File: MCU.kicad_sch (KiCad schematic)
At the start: 32 parts, among them J1 GT-USB-7010I, SW1 BOOT0, SW6 Reset, U1 STM32F722RETx, U2 AMS1117-3.3, X1 32.768kHz 7pF, Y1 16MHz 10pF

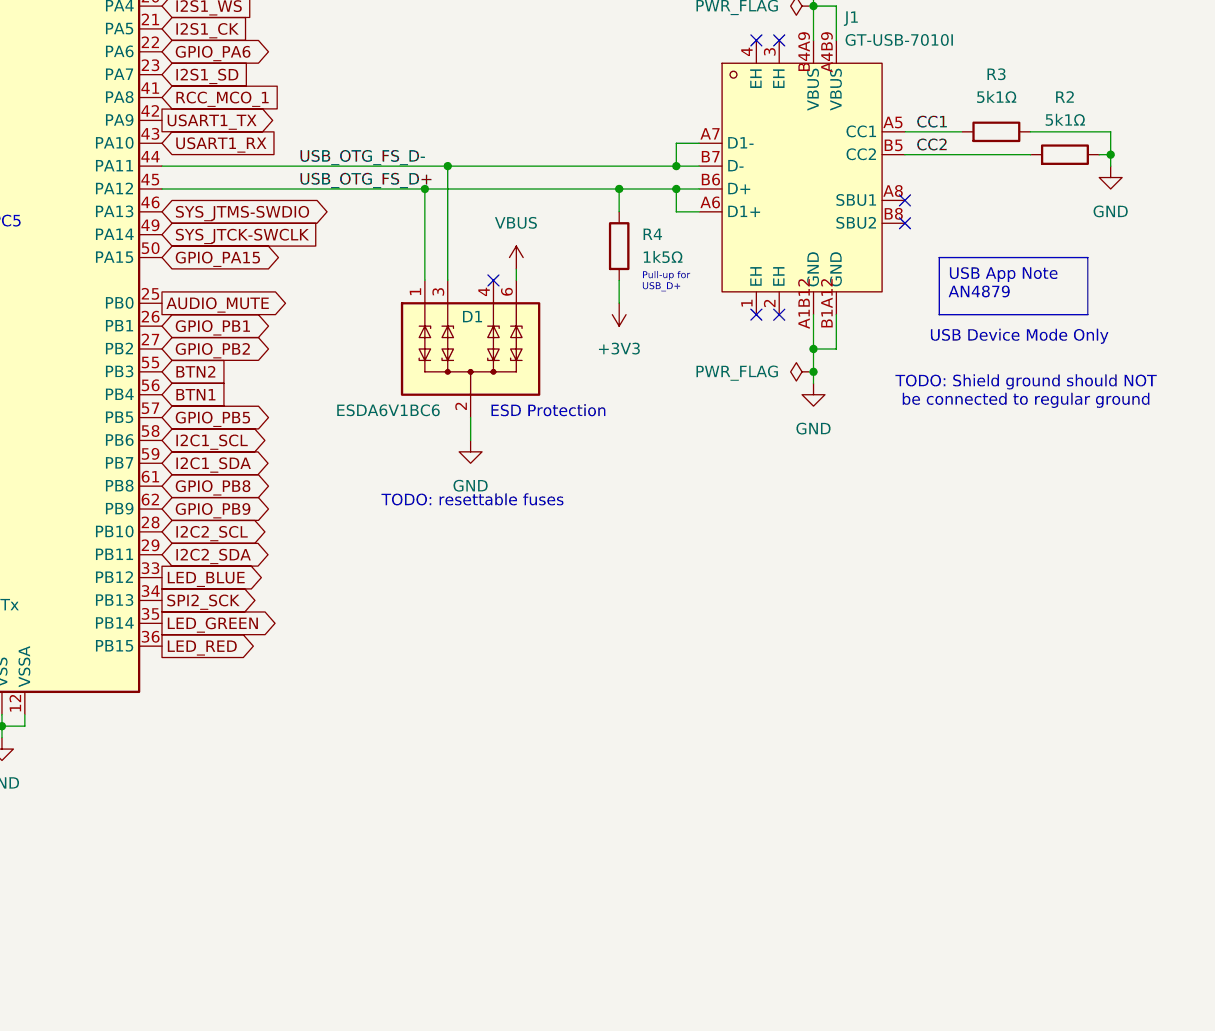
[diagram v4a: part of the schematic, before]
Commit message: Routed USB data lines; revised USB ESD for 2-layer board.
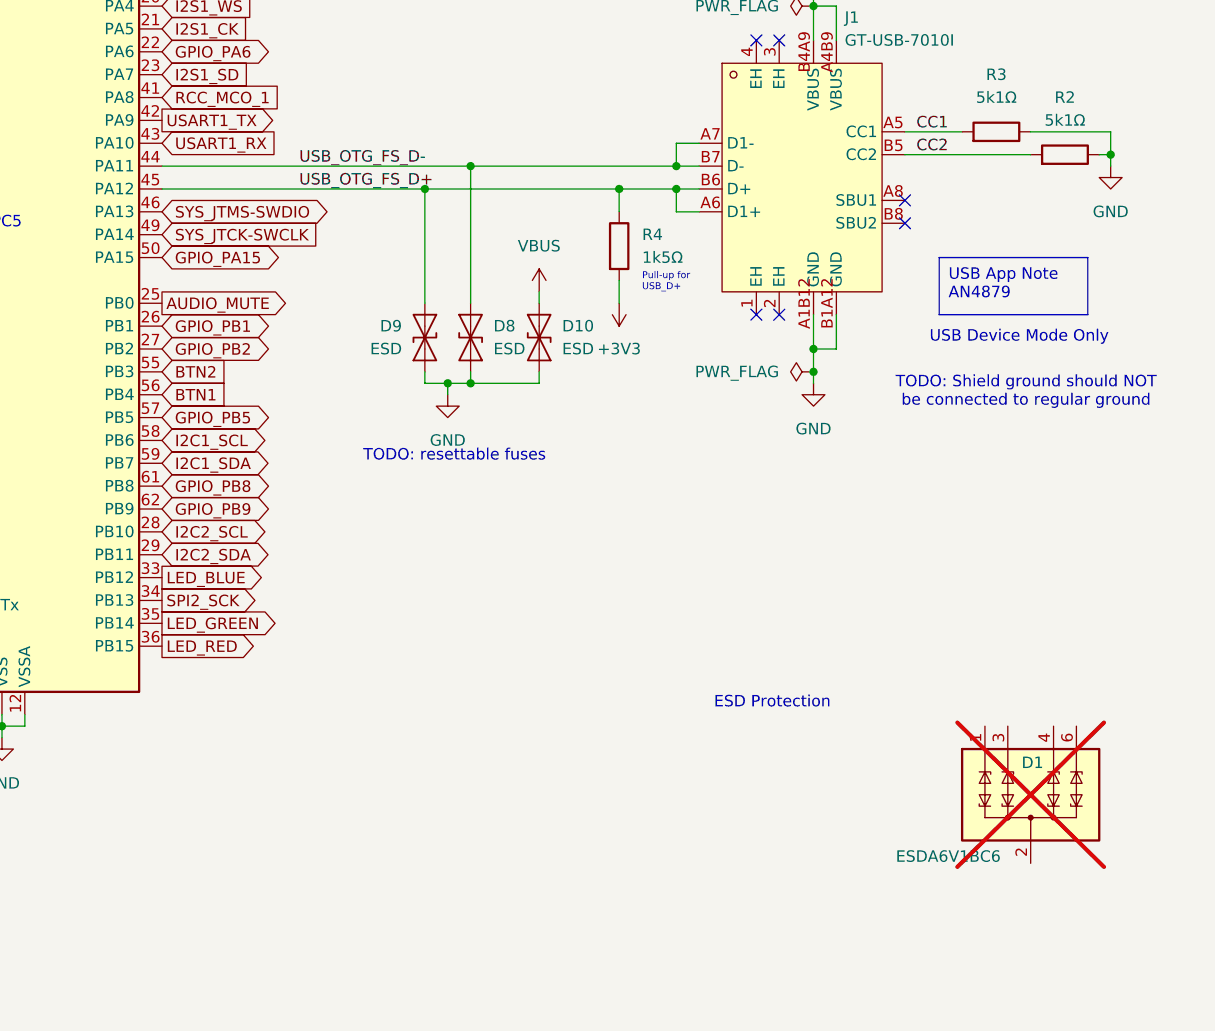
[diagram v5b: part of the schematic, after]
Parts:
- added D10, D8, D9: ESD, Diode_SMD:D_SOD-923, symbol Diode:SZESD9B5.0ST5G
- D1: now not fitted; now left out of the parts list
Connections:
- net GND: now also D10.1 (A1), D8.1 (A1), D9.1 (A1); no longer D1.2 (COM), D1.5 (COM)
- net USB_OTG_FS_D+: now also D9.2 (A2); no longer D1.1 (TVS1)
- net USB_OTG_FS_D-: now also D8.2 (A2); no longer D1.3 (TVS2)
- net VBUS: now also D10.2 (A2); no longer D1.6 (TVS4)
- new net: D1.2 (COM), D1.5 (COM)
- no-connect marks 7 -> 6

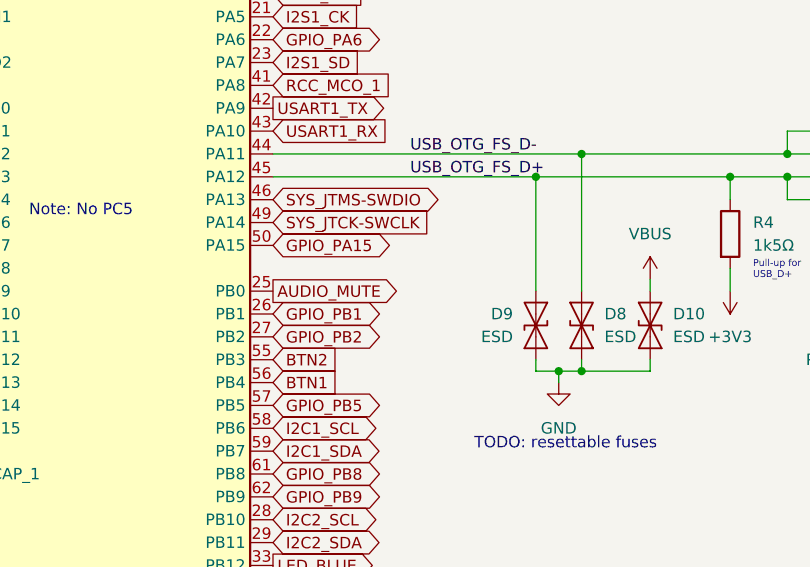
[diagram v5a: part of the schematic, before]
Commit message: Audio section is completely routed.
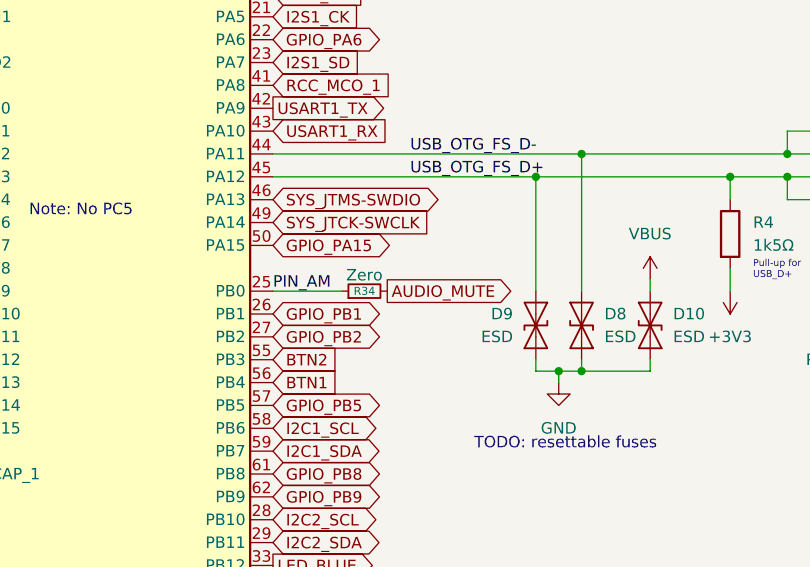
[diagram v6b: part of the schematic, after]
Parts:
- added R34: Zero, Resistor_SMD:R_1206_3216Metric, symbol Device:R_Small
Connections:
- net AUDIO_MUTE: now also R34.2; no longer U1.25 (PB0)
- new net PIN_AM: R34.1, U1.25 (PB0)
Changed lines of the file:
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@@
 	(wire
 		(pts
+			(xy 153.67 100.33) (xy 161.29 100.33)
+		)
+		(stroke
+			(width 0)
+			(type default)
+		)
+	)
+	(wire
+		(pts
 			(xy 140.97 36.83) (xy 138.43 36.83)
 		)
@@
 		)
 	)
+	(label "PIN_AM"
+		(at 153.67 100.33 0)
+		(fields_autoplaced yes)
+		(effects
+			(font
+				(size 1.27 1.27)
+			)
+			(justify left bottom)
+		)
+	)
 	(label "PWR_LED_K"
 		(at 80.01 170.18 0)
@@
 	(global_label "AUDIO_MUTE"
 		(shape output)
-		(at 153.67 100.33 0)
+		(at 166.37 100.33 0)
 		(fields_autoplaced yes)
 		(effects
@@
 		)
 		(property "Intersheetrefs" "${INTERSHEET_REFS}"
-			(at 168.1457 100.33 0)
+			(at 180.8457 100.33 0)
 			(effects
 				(font
@@
 					(unit 1)
 				)
+			)
+		)
+	)
+	(symbol
+		(lib_id "Device:R_Small")
+		(at 163.83 100.33 90)
+		(unit 1)
+		(exclude_from_sim no)
+		(in_bom yes)
+		(on_board yes)
+		(dnp no)
+		(property "Reference" "R34"
+			(at 163.83 100.33 90)
+			(effects
+				(font
+					(size 0.889 0.889)
+				)
+			)
+		)
+		(property "Value" "Zero"
+			(at 163.83 98.552 90)
+			(effects
+				(font
+					(size 1.27 1.27)
+				)
+			)
+		)
+		(property "Footprint" "Resistor_SMD:R_1206_3216Metric"
+			(at 163.83 100.33 0)
+			(effects
+				(font
+					(size 1.27 1.27)
+				)
+				(hide yes)
+			)
+		)
+		(property "Datasheet" "~"
+			(at 163.83 100.33 0)
+			(effects
+				(font
+					(size 1.27 1.27)
+				)
+				(hide yes)
+			)
+		)
+		(property "Description" "Resistor, small symbol"
+			(at 163.83 100.33 0)
+			(effects
+				(font
+					(size 1.27 1.27)
+				)
+				(hide yes)
+			)
+		)
+		(property "LCSC" ""
+			(at 163.83 100.33 0)
+			(effects
+				(font
+					(size 1.27 1.27)
+				)
+				(hide yes)
+			)
+		)
+		(property "DPFNOTES" "For Routing"
+			(at 163.83 100.33 0)
+			(effects
+				(font
+					(size 1.27 1.27)
+				)
+				(hide yes)
+			)
+		)
+		(property "DPFURL" ""
+			(at 163.83 100.33 0)
+			(effects
+				(font
+					(size 1.27 1.27)
+				)
+				(hide yes)
+			)
+		)
+		(pin "1"
+		)
+		(pin "2"
+		)
+		(instances
+			(project "stm-midi-poc1"
+				(path "/7cd74113-1f92-4dcc-8610-19aa9fc81e5f/fb10b81b-747c-4030-b31b-dec45474bc0e"
+					(reference "R34")
+					(unit 1)
+				)

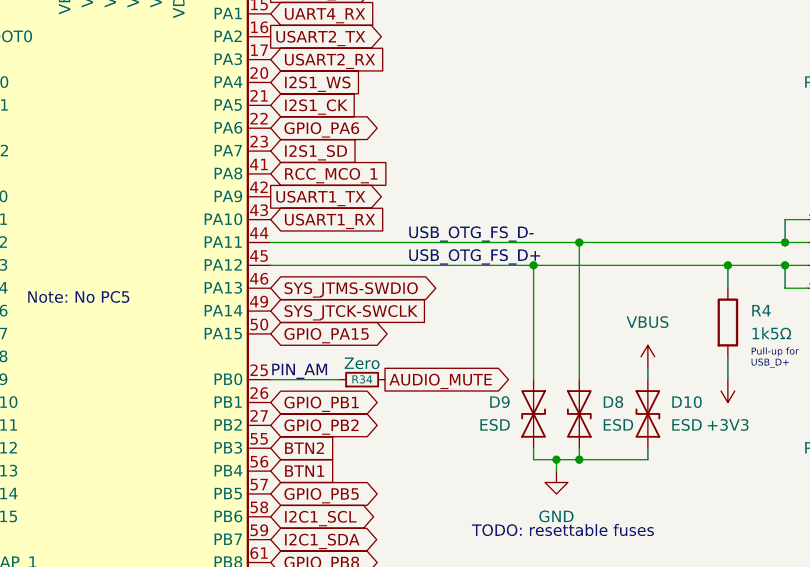
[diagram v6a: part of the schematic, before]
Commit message: Routed the SWD. I don't think it will be possible to do this on a 2-layer board anymore. I already had to use several 0-ohm resistors.
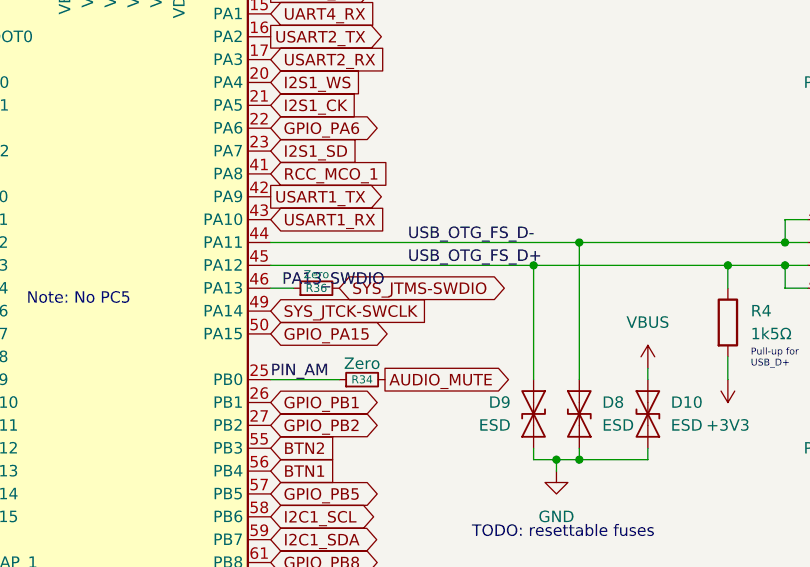
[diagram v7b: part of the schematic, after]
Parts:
- added R36: Zero, Resistor_SMD:R_2010_5025Metric, symbol Device:R_Small
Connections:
- net SYS_JTMS-SWDIO: now also R36.2; no longer U1.46 (PA13)
- new net PA13_SWDIO: R36.1, U1.46 (PA13)
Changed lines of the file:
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@@
 	(wire
 		(pts
+			(xy 156.21 90.17) (xy 153.67 90.17)
+		)
+		(stroke
+			(width 0)
+			(type default)
+		)
+	)
+	(wire
+		(pts
 			(xy 97.79 69.85) (xy 97.79 88.9)
 		)
@@
 		)
 	)
+	(label "PA13_SWDIO"
+		(at 154.94 90.17 0)
+		(fields_autoplaced yes)
+		(effects
+			(font
+				(size 1.27 1.27)
+			)
+			(justify left bottom)
+		)
+	)
 	(label "RCC_OSC32_IN"
 		(at 101.6 113.03 180)
@@
 	(global_label "SYS_JTMS-SWDIO"
 		(shape bidirectional)
-		(at 153.67 90.17 0)
+		(at 161.29 90.17 0)
 		(fields_autoplaced yes)
 		(effects
@@
 		)
 		(property "Intersheetrefs" "${INTERSHEET_REFS}"
-			(at 174.2764 90.17 0)
+			(at 181.8964 90.17 0)
 			(effects
 				(font
@@
 					(unit 1)
 				)
+			)
+		)
+	)
+	(symbol
+		(lib_id "Device:R_Small")
+		(at 158.75 90.17 90)
+		(unit 1)
+		(exclude_from_sim no)
+		(in_bom yes)
+		(on_board yes)
+		(dnp no)
+		(property "Reference" "R36"
+			(at 158.75 90.17 90)
+			(effects
+				(font
+					(size 0.889 0.889)
+				)
+			)
+		)
+		(property "Value" "Zero"
+			(at 158.75 88.646 90)
+			(effects
+				(font
+					(size 0.889 0.889)
+				)
+			)
+		)
+		(property "Footprint" "Resistor_SMD:R_2010_5025Metric"
+			(at 158.75 90.17 0)
+			(effects
+				(font
+					(size 1.27 1.27)
+				)
+				(hide yes)
+			)
+		)
+		(property "Datasheet" "~"
+			(at 158.75 90.17 0)
+			(effects
+				(font
+					(size 1.27 1.27)
+				)
+				(hide yes)
+			)
+		)
+		(property "Description" "Resistor, small symbol"
+			(at 158.75 90.17 0)
+			(effects
+				(font
+					(size 1.27 1.27)
+				)
+				(hide yes)
+			)
+		)
+		(property "LCSC" ""
+			(at 158.75 90.17 0)
+			(effects
+				(font
+					(size 1.27 1.27)
+				)
+				(hide yes)
+			)
+		)
+		(property "DPFNOTES" "For Routing"
+			(at 158.75 90.17 0)
+			(effects
+				(font
+					(size 1.27 1.27)
+				)
+				(hide yes)
+			)
+		)
+		(property "DPFURL" ""
+			(at 158.75 90.17 0)
+			(effects
+				(font
+					(size 1.27 1.27)
+				)
+				(hide yes)
+			)
+		)
+		(pin "1"
+		)
+		(pin "2"
+		)
+		(instances
+			(project "stm-midi-poc1"
+				(path "/7cd74113-1f92-4dcc-8610-19aa9fc81e5f/fb10b81b-747c-4030-b31b-dec45474bc0e"
+					(reference "R36")
+					(unit 1)
+				)

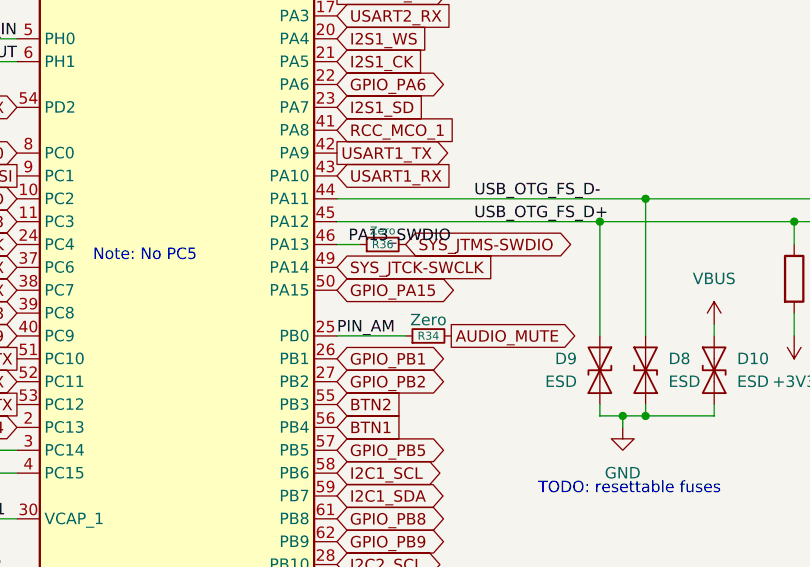
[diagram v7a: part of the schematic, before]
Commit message: Start routing through the new signal layer.
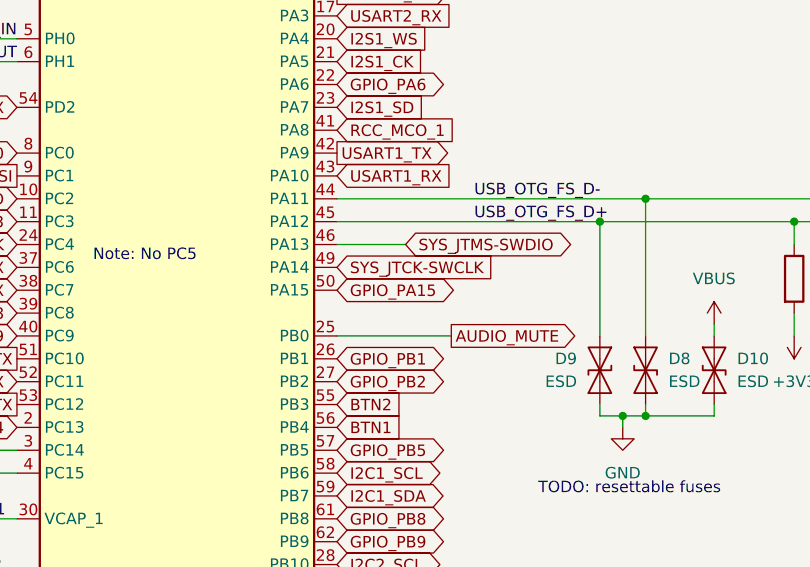
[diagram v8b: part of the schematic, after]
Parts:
- removed R34: Zero, Resistor_SMD:R_1206_3216Metric, symbol Device:R_Small
- removed R36: Zero, Resistor_SMD:R_2010_5025Metric, symbol Device:R_Small
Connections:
- net PA13_SWDIO is gone; now on net SYS_JTMS-SWDIO: U1.46 (PA13)
- net PIN_AM is gone; now on net AUDIO_MUTE: U1.25 (PB0)
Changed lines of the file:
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@@
 	(wire
 		(pts
-			(xy 153.67 100.33) (xy 161.29 100.33)
+			(xy 153.67 100.33) (xy 166.37 100.33)
 		)
 		(stroke
@@
 	(wire
 		(pts
-			(xy 156.21 90.17) (xy 153.67 90.17)
+			(xy 153.67 90.17) (xy 161.29 90.17)
 		)
 		(stroke
@@
 		)
 	)
-	(label "PIN_AM"
-		(at 153.67 100.33 0)
-		(fields_autoplaced yes)
-		(effects
-			(font
-				(size 1.27 1.27)
-			)
-			(justify left bottom)
-		)
-	)
 	(label "PWR_LED_K"
 		(at 80.01 170.18 0)
@@
 		)
 	)
-	(label "PA13_SWDIO"
-		(at 154.94 90.17 0)
-		(fields_autoplaced yes)
-		(effects
-			(font
-				(size 1.27 1.27)
-			)
-			(justify left bottom)
-		)
-	)
 	(label "RCC_OSC32_IN"
 		(at 101.6 113.03 180)
@@
 	)
 	(symbol
-		(lib_id "Device:R_Small")
-		(at 158.75 90.17 90)
-		(unit 1)
-		(exclude_from_sim no)
-		(in_bom yes)
-		(on_board yes)
-		(dnp no)
-		(property "Reference" "R36"
-			(at 158.75 90.17 90)
-			(effects
-				(font
-					(size 0.889 0.889)
-				)
-			)
-		)
-		(property "Value" "Zero"
-			(at 158.75 88.646 90)
-			(effects
-				(font
-					(size 0.889 0.889)
-				)
-			)
-		)
-		(property "Footprint" "Resistor_SMD:R_2010_5025Metric"
-			(at 158.75 90.17 0)
-			(effects
-				(font
-					(size 1.27 1.27)
-				)
-				(hide yes)
-			)
-		)
-		(property "Datasheet" "~"
-			(at 158.75 90.17 0)
-			(effects
-				(font
-					(size 1.27 1.27)
-				)
-				(hide yes)
-			)
-		)
-		(property "Description" "Resistor, small symbol"
-			(at 158.75 90.17 0)
-			(effects
-				(font
-					(size 1.27 1.27)
-				)
-				(hide yes)
-			)
-		)
-		(property "LCSC" ""
-			(at 158.75 90.17 0)
-			(effects
-				(font
-					(size 1.27 1.27)
-				)
-				(hide yes)
-			)
-		)
-		(property "DPFNOTES" "For Routing"
-			(at 158.75 90.17 0)
-			(effects
-				(font
-					(size 1.27 1.27)
-				)
-				(hide yes)
-			)
-		)
-		(property "DPFURL" ""
-			(at 158.75 90.17 0)
-			(effects
-				(font
-					(size 1.27 1.27)
-				)
-				(hide yes)
-			)
-		)
-		(pin "1"
-		)
-		(pin "2"
-		)
-		(instances
-			(project "stm-midi-poc1"
-				(path "/7cd74113-1f92-4dcc-8610-19aa9fc81e5f/fb10b81b-747c-4030-b31b-dec45474bc0e"
-					(reference "R36")
-					(unit 1)
-				)
-			)
-		)
-	)
-	(symbol
 		(lib_id "power:GND")
 		(at 226.06 109.22 0)
@@
 					(unit 1)
 				)
-			)
-		)
-	)
-	(symbol
-		(lib_id "Device:R_Small")
-		(at 163.83 100.33 90)
-		(unit 1)
-		(exclude_from_sim no)
-		(in_bom yes)
-		(on_board yes)
-		(dnp no)
-		(property "Reference" "R34"
-			(at 163.83 100.33 90)
-			(effects
-				(font
-					(size 0.889 0.889)
-				)
-			)
-		)
-		(property "Value" "Zero"
-			(at 163.83 98.552 90)
-			(effects
-				(font
-					(size 1.27 1.27)
-				)
-			)
-		)
-		(property "Footprint" "Resistor_SMD:R_1206_3216Metric"
-			(at 163.83 100.33 0)
-			(effects
-				(font
-					(size 1.27 1.27)
-				)
-				(hide yes)
-			)
-		)
-		(property "Datasheet" "~"
-			(at 163.83 100.33 0)
-			(effects
-				(font
-					(size 1.27 1.27)
-				)
-				(hide yes)
-			)
-		)
-		(property "Description" "Resistor, small symbol"
-			(at 163.83 100.33 0)
-			(effects
-				(font
-					(size 1.27 1.27)
-				)
-				(hide yes)
-			)
-		)
-		(property "LCSC" ""
-			(at 163.83 100.33 0)
-			(effects
-				(font
-					(size 1.27 1.27)
-				)
-				(hide yes)
-			)
-		)
-		(property "DPFNOTES" "For Routing"
-			(at 163.83 100.33 0)
-			(effects
-				(font
-					(size 1.27 1.27)
-				)
-				(hide yes)
-			)
-		)
-		(property "DPFURL" ""
-			(at 163.83 100.33 0)
-			(effects
-				(font
-					(size 1.27 1.27)
-				)
-				(hide yes)
-			)
-		)
-		(pin "1"
-		)
-		(pin "2"
-		)
-		(instances
-			(project "stm-midi-poc1"
-				(path "/7cd74113-1f92-4dcc-8610-19aa9fc81e5f/fb10b81b-747c-4030-b31b-dec45474bc0e"
-					(reference "R34")
-					(unit 1)
-				)
